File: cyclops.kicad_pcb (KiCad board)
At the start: 2 copper layers, 285 x 94.6 mm, 139 parts, among them J1 USB_mini_micro_B, K1 ESC, K10 KEYSW, K11 KEYSW, K12 KEYSW, K13 KEYSW, K14 backspace, K15 tab, K16 KEYSW, K17 KEYSW, K18 KEYSW, K19 KEYSW, K2 1, K20 KEYSW, K21 KEYSW, K22 KEYSW, K23 KEYSW, K24 KEYSW, K25 KEYSW, K26 KEYSW, K27 KEYSW, K28 Lock, K29 KEYSW, K3 KEYSW, K30 KEYSW, K31 KEYSW, K32 KEYSW, K33 KEYSW, K34 KEYSW, K35 KEYSW, K36 KEYSW, K37 KEYSW, K38 KEYSW, K39 KEYSW, K4 KEYSW, K40 KEYSW, K41 Shift, K42 KEYSW, K43 KEYSW, K44 KEYSW, K45 KEYSW, K46 KEYSW, K47 KEYSW, K48 KEYSW, K49 KEYSW, K5 KEYSW, K50 KEYSW, K51 KEYSW, K52 KEYSW, K53 Shift, K54 Ctrl, K55 alt, K56 opt, K57 space, K58 cmd, K59 alt, K6 KEYSW, K60 ctrl, K61 enter, K7 KEYSW, K8 KEYSW, K9 KEYSW, SW1 SW_Push, U1 ATMEGA32U2, X1 XTAL_GND

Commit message: PCB layout complete
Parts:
- C1, C2, C3, C4, C5, C6, C7, C8, D1, D10, D11, D12, D13, D14, D15, D16, D17, D18, D19, D2, D20, D21, D22, D23, D24, D25, D26, D27, D28, D29, D3, D30, D31, D32, D33, D34, D35, D36, D37, D38, D39, D4, D40, D41, D42, D43, D44, D45, D46, D47, D48, D49, D5, D50, D51, D52, D53, D54, D55, D56, D57, D58, D59, D6, D60, D61, D7, D8, D9, J1, K1, R1, R2, R3, R4, SW1, U1: moved to B.Cu
- X1: footprint Crystals:Crystal_SMD_0603-4pin_6.0x3.5mm_HandSoldering -> Crystals:Crystal_SMD_SeikoEpson_FA238-4pin_3.2x2.5mm_HandSoldering; moved to B.Cu
- moved D60 199.6 mm to (332.1, 183.3), turned to 90 degrees
- moved D61 190.4 mm to (336.9, 132.5), turned to 90 degrees
- moved D53 183.9 mm to (322.6, 164.3), turned to 90 degrees
- moved D14 181.3 mm to (329.8, 107.1), turned to 90 degrees
- moved K40 180.8 mm to (324.8, 145.2)
- moved D59 175.8 mm to (306.0, 183.3), turned to 90 degrees
- moved D40 174.0 mm to (317.8, 145.2), turned to 90 degrees
- moved D27 165.9 mm to (313.0, 126.1), turned to 90 degrees
- moved K39 162.4 mm to (305.8, 145.2)
- moved K52 159.2 mm to (296.3, 164.3)
- moved D39 155.6 mm to (298.8, 145.2), turned to 90 degrees
- moved D13 155.1 mm to (303.5, 107.1), turned to 90 degrees
- moved D58 152.8 mm to (279.8, 183.3), turned to 90 degrees
- moved D52 152.7 mm to (289.3, 164.3), turned to 90 degrees
- moved D26 147.0 mm to (294.0, 126.2), turned to 90 degrees
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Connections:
- U1 pad 1: Net-(C7-Pad1) -> Net-(C8-Pad1)
- U1 pad 2: Net-(C8-Pad1) -> Net-(C7-Pad1)

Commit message: pcb complete
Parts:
- removed REF**: 60_Outline, local_lib:60_Outline
- J1: footprint keyboard_parts:USB_miniB_hirose_5ST_hand -> keyboard_parts:USB_miniB_hirose_5S8
- moved C1 131.9 mm to (171.1, 172.5), turned to 90 degrees
- moved C5 126.0 mm to (160.0, 187.1), turned to 180 degrees
- moved C4 122.4 mm to (160.0, 185.1), turned to 180 degrees
- moved C3 27.3 mm to (81.6, 108.5), turned to 180 degrees
- moved C2 26.8 mm to (81.6, 106.5), turned to 180 degrees
- moved C6 1.69 mm to (169.1, 190.5), turned to 180 degrees
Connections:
- C6 pad 2: Net-(C6-Pad2) -> GND
- D22 pad 1: (no net) -> /ROW1
- J1 pad 5: Net-(C6-Pad2) -> GND
- J1 pad 6: Net-(C6-Pad2) -> GND
- U1 pad 10: /COL0 -> /COL3
- U1 pad 11: /COL1 -> /ROW2
- U1 pad 12: /COL2 -> /ROW3
- U1 pad 14: /COL3 -> /COL4
- U1 pad 15: /COL4 -> /COL5
- U1 pad 16: /COL5 -> /COL6
- U1 pad 17: (no net) -> /COL7
- U1 pad 18: /COL13 -> /COL8
- U1 pad 19: /COL12 -> /COL9
- U1 pad 20: /COL11 -> /COL10
- U1 pad 21: /COL10 -> /COL11
- U1 pad 22: /COL9 -> /COL13
- U1 pad 23: /COL8 -> /COL12
- U1 pad 25: /COL7 -> (no net)
- U1 pad 26: /COL6 -> /ROW4
- U1 pad 28: Net-(C6-Pad2) -> GND
- U1 pad 5: /ROW0 -> /ROW1
- U1 pad 6: /ROW1 -> /ROW0
- U1 pad 7: /ROW2 -> /COL1
- U1 pad 8: /ROW3 -> /COL0
- U1 pad 9: /ROW4 -> /COL2
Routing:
- net /ROW0: track 0.00 -> 341.8 mm, vias 0 -> 4
- net /ROW4: track 0.00 -> 331.6 mm
- net /ROW1: track 0.00 -> 296.6 mm, vias 0 -> 2
- net /ROW2: track 0.00 -> 275.9 mm, vias 0 -> 2
- net /COL13: track 0.00 -> 267.0 mm
- net /ROW3: track 0.00 -> 264.0 mm
- net /COL12: track 0.00 -> 262.8 mm
- net VCC: track 0.00 -> 230.4 mm, vias 0 -> 4
- net /COL11: track 0.00 -> 226.4 mm, vias 0 -> 1
- net Net-(R3-Pad2): track 0.00 -> 208.5 mm, vias 0 -> 2
- net /COL10: track 0.00 -> 196.6 mm, vias 0 -> 1
- net /COL0: track 0.00 -> 177.1 mm, vias 0 -> 1
- net Net-(R1-Pad1): track 0.00 -> 173.0 mm, vias 0 -> 2
- net Net-(R2-Pad1): track 0.00 -> 172.4 mm, vias 0 -> 4
- net /COL9: track 0.00 -> 163.5 mm, vias 0 -> 1
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- added copper zone on B.Cu, net GND
- added copper zone on F.Cu, net GND
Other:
- board outline removed

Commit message: revised pcb
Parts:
- moved C1 12.6 mm to (158.5, 172.0), turned to 180 degrees
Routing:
- net GND: track 32.9 -> 99.6 mm

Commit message: pcb minor fixes
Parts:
- removed C7, C8: 22p, Capacitors_SMD:C_0805_HandSoldering
- C3: value 0.1u -> 4.7u
- C4: value 0.1u -> 1u
- C5: value 4.7u -> 22p
- C6: value 1u -> 22p
- moved C2 113.5 mm to (163.9, 184.7)
- moved C3 113.4 mm to (163.9, 186.5)
- moved C5 15.0 mm to (167.6, 174.1), turned to 135 degrees
- moved C6 12.9 mm to (161.5, 180.0), turned to 135 degrees
- moved C1 12.7 mm to (171.2, 172.4)
- moved C4 10.6 mm to (169.1, 190.4)
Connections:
- C4 pad 1: VCC -> Net-(C4-Pad1)
- C5 pad 1: VCC -> Net-(C5-Pad1)
- U1 pad 1: Net-(C8-Pad1) -> Net-(C6-Pad1)
- U1 pad 2: Net-(C7-Pad1) -> Net-(C5-Pad1)
- U1 pad 27: Net-(C6-Pad1) -> Net-(C4-Pad1)
- X1 pad 1: Net-(C7-Pad1) -> Net-(C5-Pad1)
- X1 pad 2: Net-(C8-Pad1) -> Net-(C6-Pad1)
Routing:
- net GND: track 99.6 -> 45.9 mm
- net Net-(C8-Pad1): track 8.41 -> 0.00 mm
- net Net-(C7-Pad1): track 8.20 -> 0.00 mm
- net Net-(C5-Pad1): track 0.00 -> 8.20 mm
- net VCC: track 230.7 -> 224.0 mm
- net Net-(C4-Pad1): track 0.00 -> 4.48 mm
- net Net-(C6-Pad1): track 4.48 -> 8.41 mm
- net Net-(R2-Pad1): track 172.4 -> 170.9 mm, vias 4 -> 2

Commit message: Move mcu components out temporarily
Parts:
- moved C1 23.2 mm to (171.8, 195.7)
- moved C2 23.2 mm to (164.4, 207.9)
- moved C3 23.2 mm to (164.4, 209.7)
- moved C4 23.2 mm to (169.6, 213.7)
- moved R3 23.2 mm to (182.7, 212.8)
- moved R4 23.2 mm to (182.7, 198.1)
- moved U1 23.2 mm to (174.1, 205.8), turned to 0 degrees
- moved X1 23.2 mm to (165.0, 200.3), turned to 0 degrees
- moved C5 23.2 mm to (168.1, 197.4), turned to 0 degrees
- moved C6 21.0 mm to (159.8, 200.9), turned to 0 degrees
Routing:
- net VCC: track 224.0 -> 155.0 mm, vias 4 -> 2
- net GND: track 45.9 -> 12.8 mm
- net /COL1: track 156.6 -> 136.9 mm
- net /COL0: track 177.5 -> 163.6 mm
- net /COL4: track 103.4 -> 93.1 mm, vias 2 -> 1
- net /COL5: track 90.4 -> 80.2 mm
- net /COL3: track 121.7 -> 112.3 mm
- net Net-(C6-Pad1): track 8.41 -> 0.00 mm
- net Net-(C5-Pad1): track 8.20 -> 0.00 mm
- net /COL2: track 154.7 -> 146.7 mm
- net Net-(R3-Pad2): track 208.5 -> 201.4 mm, vias 2 -> 1
- net Net-(R4-Pad1): track 6.65 -> 0.00 mm
- net /ROW4: track 331.6 -> 325.2 mm
- net /ROW1: track 296.5 -> 290.2 mm, vias 2 -> 1
- net /ROW0: track 341.5 -> 336.5 mm, vias 4 -> 3
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
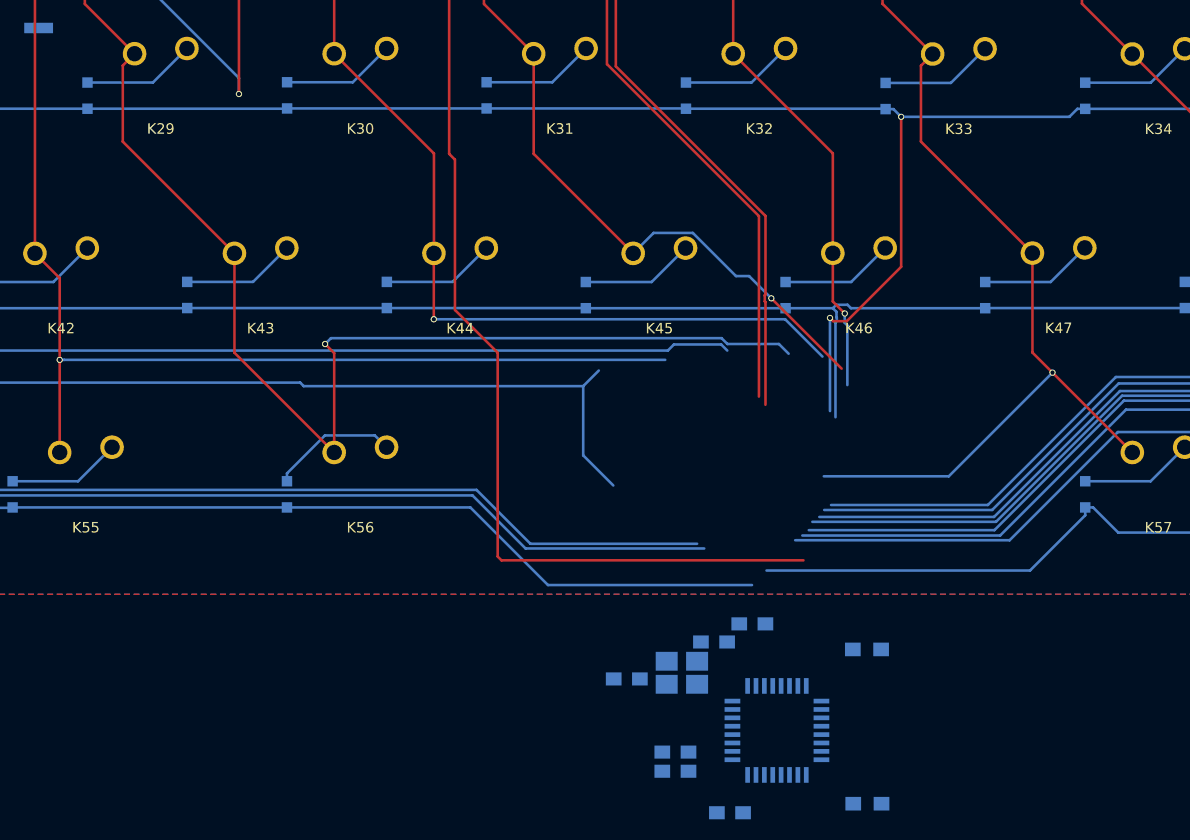
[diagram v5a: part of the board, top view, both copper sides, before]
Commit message: Move MCU back into place
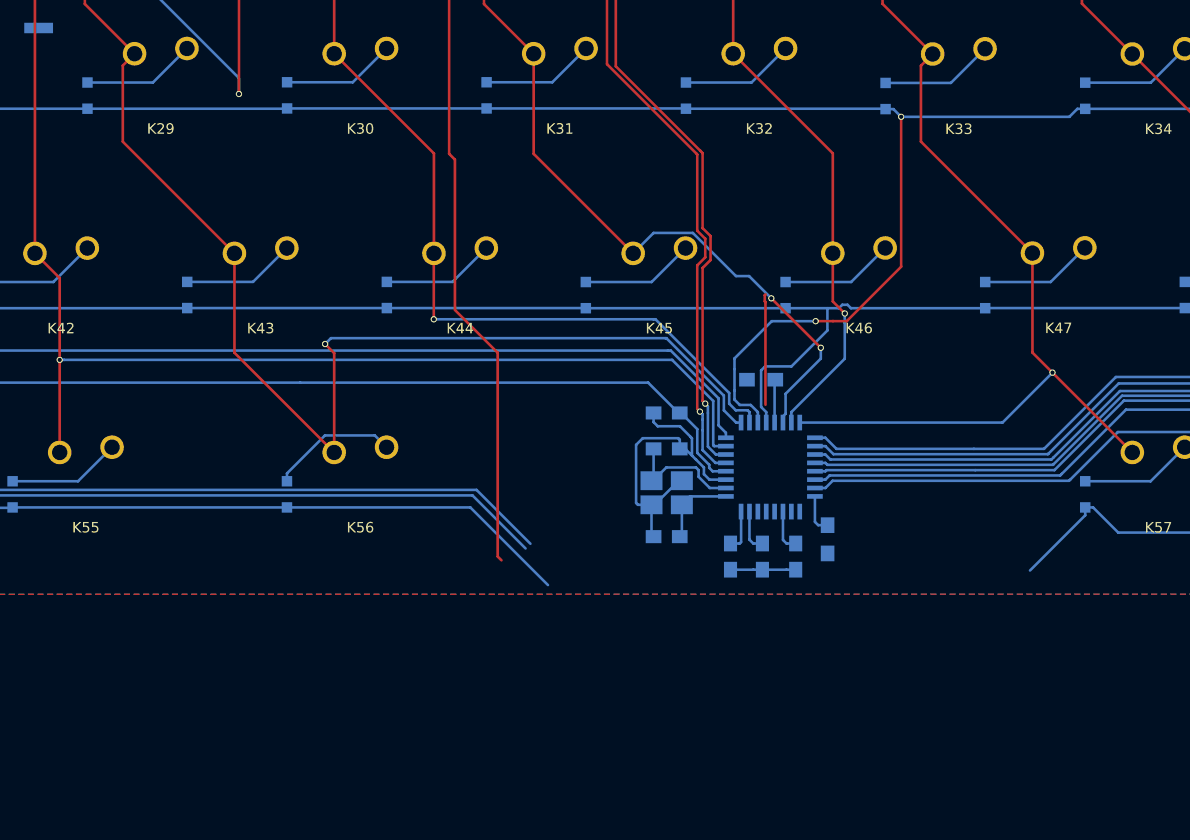
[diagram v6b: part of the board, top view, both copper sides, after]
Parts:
- X1: value XTAL_GND -> Crystal_3225; footprint Crystals:Crystal_SMD_SeikoEpson_FA238-4pin_3.2x2.5mm_HandSoldering -> Crystals:Crystal_SMD_3225-4pin_3.2x2.5mm_HandSoldering
- moved R4 27.7 mm to (172.6, 172.3), turned to 180 degrees
- moved R3 25.5 mm to (178.9, 187.6), turned to 90 degrees
- moved C4 25.3 mm to (175.9, 189.2), turned to 270 degrees
- moved U1 25.2 mm to (173.5, 180.7)
- moved C3 22.1 mm to (172.7, 189.2), turned to 270 degrees
- moved C1 21.7 mm to (163.6, 175.5)
- moved C2 19.4 mm to (169.7, 189.2), turned to 270 degrees
- moved C5 19.0 mm to (163.6, 178.9)
- moved X1 17.3 mm to (163.6, 183.1), turned to 180 degrees
- moved C6 14.1 mm to (163.6, 187.3), turned to 180 degrees
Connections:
- J1 pad 4: (no net) -> Net-(J1-Pad4)
- U1 pad 25: (no net) -> Net-(U1-Pad25)
- X1 pad 1: Net-(C5-Pad1) -> Net-(C6-Pad1)
- X1 pad 2: Net-(C6-Pad1) -> GND
- X1 pad 3: GND -> Net-(C5-Pad1)
- X1 pad 4: (no net) -> GND
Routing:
- net /ROW4: track 325.2 -> 280.5 mm
- net GND: track 12.8 -> 51.2 mm
- net Net-(R3-Pad2): track 201.4 -> 176.3 mm
- net Net-(R1-Pad1): track 169.0 -> 152.0 mm
- net Net-(R2-Pad1): track 166.3 -> 150.4 mm
- net /ROW0: track 336.5 -> 351.2 mm, vias 3 -> 4
- net VCC: track 155.0 -> 168.8 mm
- net Net-(C5-Pad1): track 0.00 -> 11.9 mm
- net /COL1: track 136.9 -> 148.5 mm
- net /ROW2: track 271.1 -> 280.3 mm
- net Net-(C6-Pad1): track 0.00 -> 7.66 mm
- net /ROW1: track 290.2 -> 296.4 mm, vias 1 -> 2
- net /COL4: track 93.1 -> 98.9 mm, vias 1 -> 2
- net /COL5: track 80.2 -> 85.8 mm
- net /COL0: track 163.6 -> 168.2 mm
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
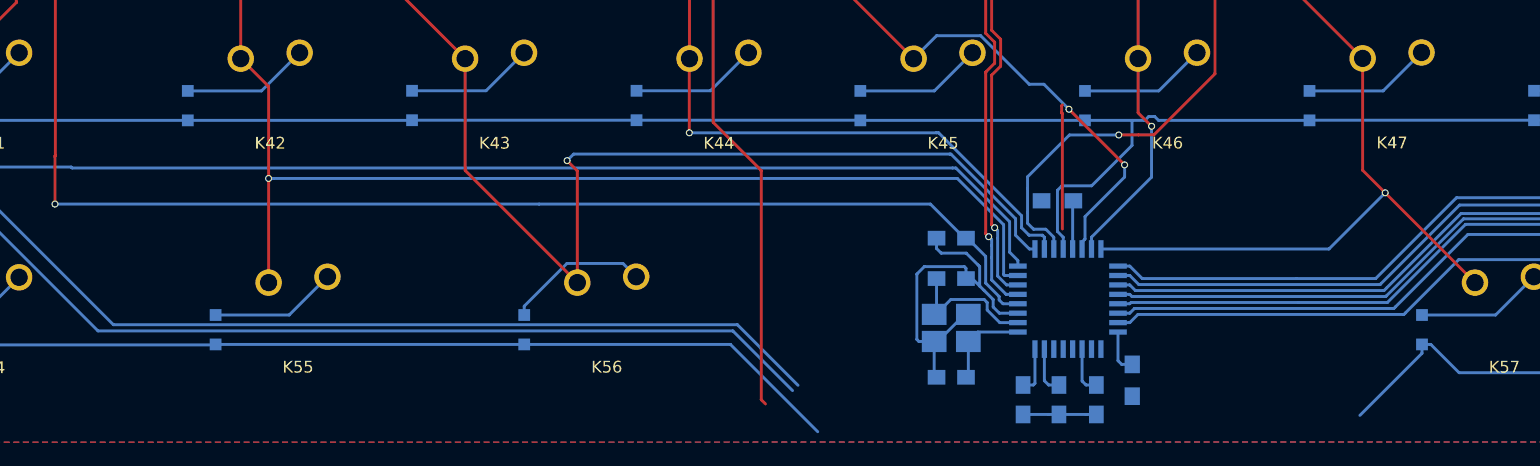
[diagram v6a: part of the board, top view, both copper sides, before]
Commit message: Move MCU up
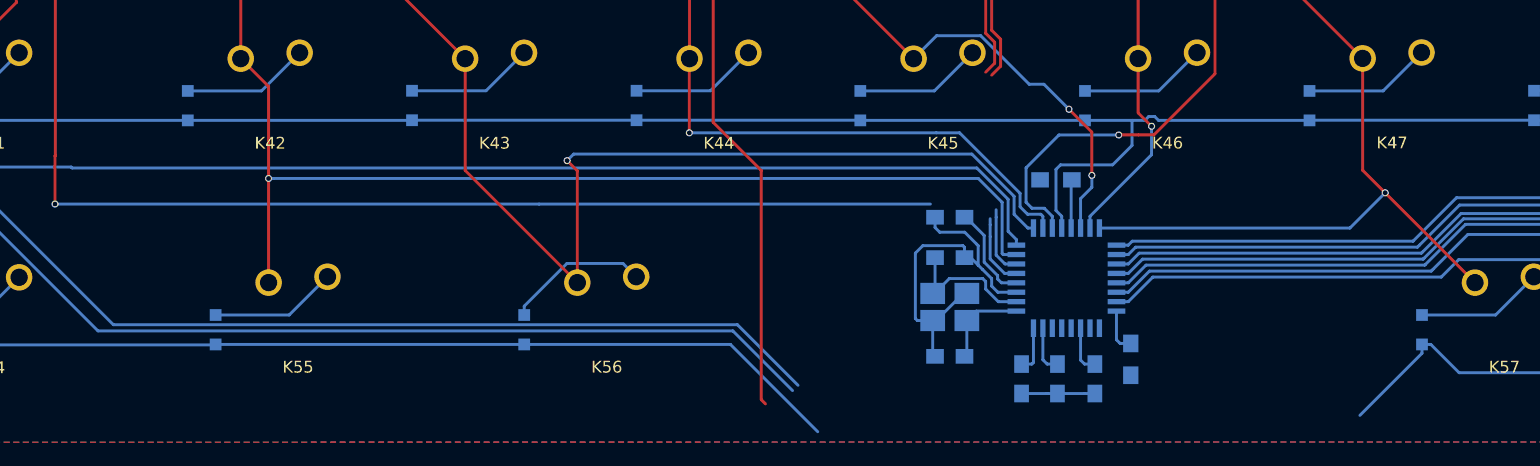
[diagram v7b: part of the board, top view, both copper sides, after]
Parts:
- moved R3 1.78 mm to (178.8, 185.8)
- moved C1 1.78 mm to (163.4, 173.7)
- moved C5 1.78 mm to (163.4, 177.2)
- moved C2 1.78 mm to (169.5, 187.5)
- moved C3 1.78 mm to (172.6, 187.5)
- moved C4 1.78 mm to (175.8, 187.5)
- moved U1 1.78 mm to (173.4, 178.9)
- moved C6 1.78 mm to (163.4, 185.5)
- moved R4 1.78 mm to (172.5, 170.6)
- moved X1 1.78 mm to (163.4, 181.4)
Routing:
- net /ROW0: track 351.2 -> 327.2 mm, vias 4 -> 3
- net /ROW1: track 296.4 -> 282.0 mm, vias 2 -> 1
- net VCC: track 168.8 -> 164.7 mm
- net /COL4: track 98.9 -> 94.9 mm
- net /COL5: track 85.8 -> 84.1 mm
- net /COL7: track 121.4 -> 119.9 mm
- net /COL8: track 141.6 -> 140.3 mm
- net /ROW2: track 280.3 -> 279.1 mm
- net /COL9: track 160.9 -> 159.9 mm
- net /COL0: track 168.2 -> 167.4 mm
- net /COL3: track 109.1 -> 108.3 mm
- net /COL1: track 148.5 -> 147.7 mm
- net /COL2: track 145.7 -> 145.0 mm
- net /COL10: track 193.3 -> 192.5 mm
- net /COL13: track 262.5 -> 261.8 mm
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
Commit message: Finish MCU breakout
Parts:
- moved C3 0.89 mm to (171.7, 187.5)
- moved C2 0.76 mm to (168.8, 187.5)
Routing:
- net /ROW4: track 280.5 -> 333.7 mm
- net Net-(R1-Pad1): track 152.0 -> 183.0 mm
- net GND: track 51.2 -> 81.6 mm, vias 0 -> 4
- net Net-(R2-Pad1): track 150.4 -> 180.2 mm
- net VCC: track 164.7 -> 189.6 mm, vias 2 -> 4
- net Net-(R3-Pad2): track 176.3 -> 198.6 mm, vias 1 -> 2
- net /ROW1: track 282.0 -> 296.3 mm, vias 1 -> 2
- net /ROW0: track 327.2 -> 339.9 mm, vias 3 -> 4
- net /COL6: track 116.5 -> 117.0 mm
